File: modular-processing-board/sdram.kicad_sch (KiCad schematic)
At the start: 18 parts, among them U301 W9825G6KH-6, U302 W9825G6KH-6

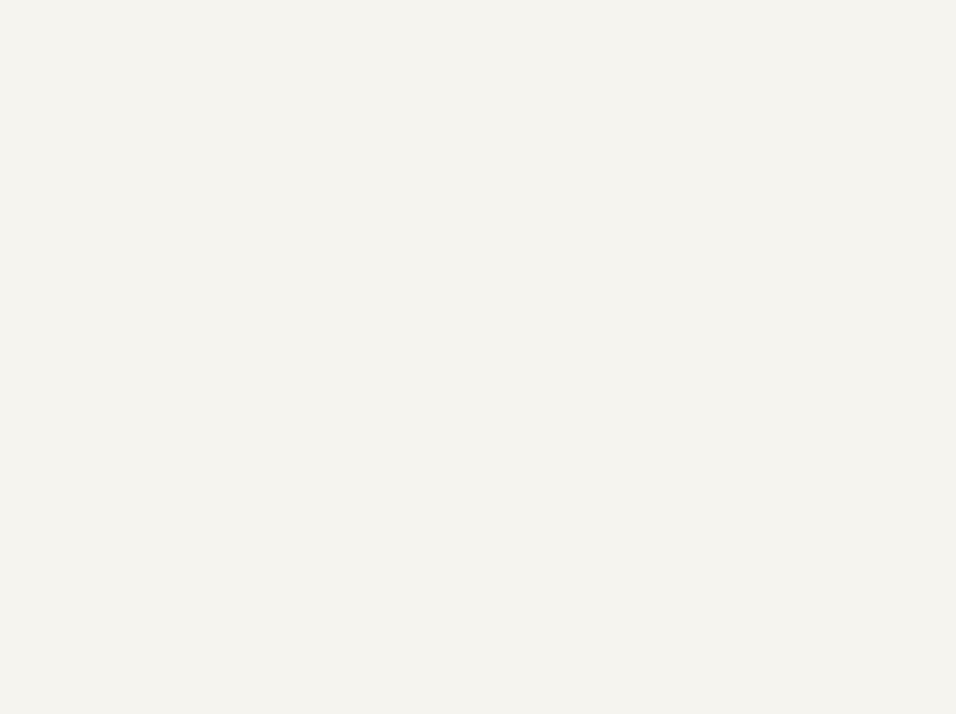
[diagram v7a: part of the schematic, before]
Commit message: checked timing for sdram, routing
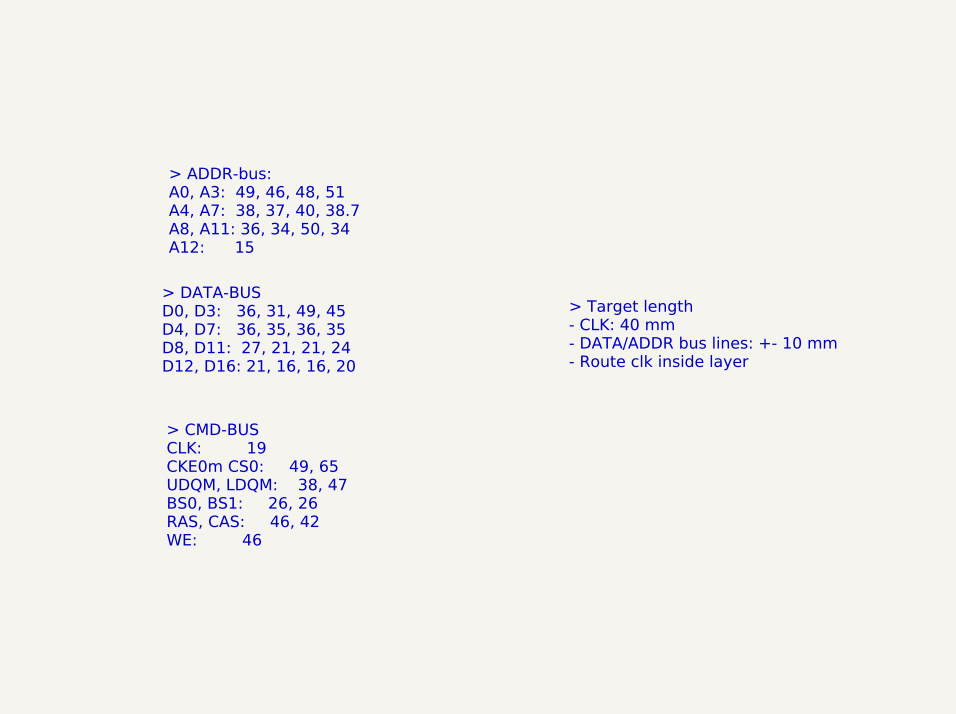
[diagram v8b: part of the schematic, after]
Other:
- note added: "> ADDR-bus: A0, A3: 49, 46, 48, 51 A4, A7: 38, 37, 40, 38.7 A8, A11: 36, 34, 50, 34 A12: 15"
- note added: "> CMD-BUS CLK: 19 CKE0m CS0: 49, 65 UDQM, LDQM: 38, 47 BS0, BS1: 26, 26 RAS, CAS: 46, 42 WE: 46"
- note added: "> DATA-BUS D0, D3: 36, 31, 49, 45 D4, D7: 36, 35, 36, 35 D8, D11: 27, 21, 21, 24 D12, D16: 21, 16, 16, 20"
- note added: "> Target length - CLK: 40 mm - DATA/ADDR bus lines: +- 10 mm - Route clk inside layer"
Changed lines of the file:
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@@
+		)
+	)
+	(text "> DATA-BUS\nD0, D3:   36, 31, 49, 45\nD4, D7:   36, 35, 36, 35\nD8, D11:  27, 21, 21, 24\nD12, D16: 21, 16, 16, 20\n"
+		(exclude_from_sim no)
+		(at 308.61 86.868 0)
+		(effects
+			(font
+				(size 1.27 1.27)
+			)
+			(justify left)
+		)
+	)
+	(text "> Target length\n- CLK: 40 mm\n- DATA/ADDR bus lines: +- 10 mm\n- Route clk inside layer"
+		(exclude_from_sim no)
+		(at 353.822 87.376 0)
+		(effects
+			(font
+				(size 1.27 1.27)
+			)
+			(justify left)
+		)
+	)
+	(text "> CMD-BUS\nCLK: 		19\nCKE0m CS0: 	49, 65\nUDQM, LDQM:	38, 47\nBS0, BS1: 	26, 26\nRAS, CAS: 	46, 42\nWE: 		46"
+		(exclude_from_sim no)
+		(at 309.118 104.14 0)
+		(effects
+			(font
+				(size 1.27 1.27)
+			)
+			(justify left)
 		)
 	)
@@
 		)
 	)
+	(text "> ADDR-bus:\nA0, A3:  49, 46, 48, 51\nA4, A7:  38, 37, 40, 38.7\nA8, A11: 36, 34, 50, 34\nA12: 	 15\n"
+		(exclude_from_sim no)
+		(at 309.372 73.66 0)
+		(effects
+			(font
+				(size 1.27 1.27)
+			)
+			(justify left)
+		)
+	)
